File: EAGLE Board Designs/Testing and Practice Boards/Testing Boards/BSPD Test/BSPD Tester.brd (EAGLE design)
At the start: 26.3 x 62.2 mm, 43 parts, among them J1 JUMPER.1, J10 JUMPER.1, J11 JUMPER.1, J12 JUMPER.1, J13 JUMPER.1, J14 JUMPER.1, J15 JUMPER.1, J16 JUMPER.1, J17 JUMPER.1, J18 JUMPER.1, J19 JUMPER.1, J2 JUMPER.1, J20 JUMPER.1, J21 JUMPER.1, J3 JUMPER.1, J4 JUMPER.1, J5 JUMPER.1, J6 JUMPER.1, J7 JUMPER.1, J8 JUMPER.1, J9 JUMPER.1, X1 CONNECTOR-4NANO-FIT-VERTICAL-4

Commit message: final uplaod of rev1 BSPD test board
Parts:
- moved J21 17.8 mm to (3.81, 62.2), turned to 180 degrees
- moved J19 16.3 mm to (15.2, 73.7)
- moved J14 3.81 mm to (3.81, 54.6)
- moved J15 3.81 mm to (3.81, 50.8)
- moved J17 3.81 mm to (3.81, 43.2)
- moved J18 3.81 mm to (3.81, 39.4)
- moved R15 3.81 mm to (8.89, 54.6)
- moved R16 3.81 mm to (8.89, 50.8)
- moved R18 3.81 mm to (8.89, 43.2)
- moved R19 3.81 mm to (8.89, 39.4)
- moved J13 3.81 mm to (3.81, 58.4)
- moved J16 3.81 mm to (3.81, 47.0)
- moved R14 3.81 mm to (8.89, 58.4)
- moved R17 3.81 mm to (8.89, 47.0)
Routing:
- net STUPID2: track 19.0 -> 51.0 mm
- net CURRENT: track 8.02 -> 19.1 mm
- net VCC: track 124.9 -> 131.8 mm
- net STUPID: track 52.0 -> 58.8 mm
- net N$20: track 0.00 -> 6.13 mm
- net BRAKE: track 24.7 -> 21.0 mm

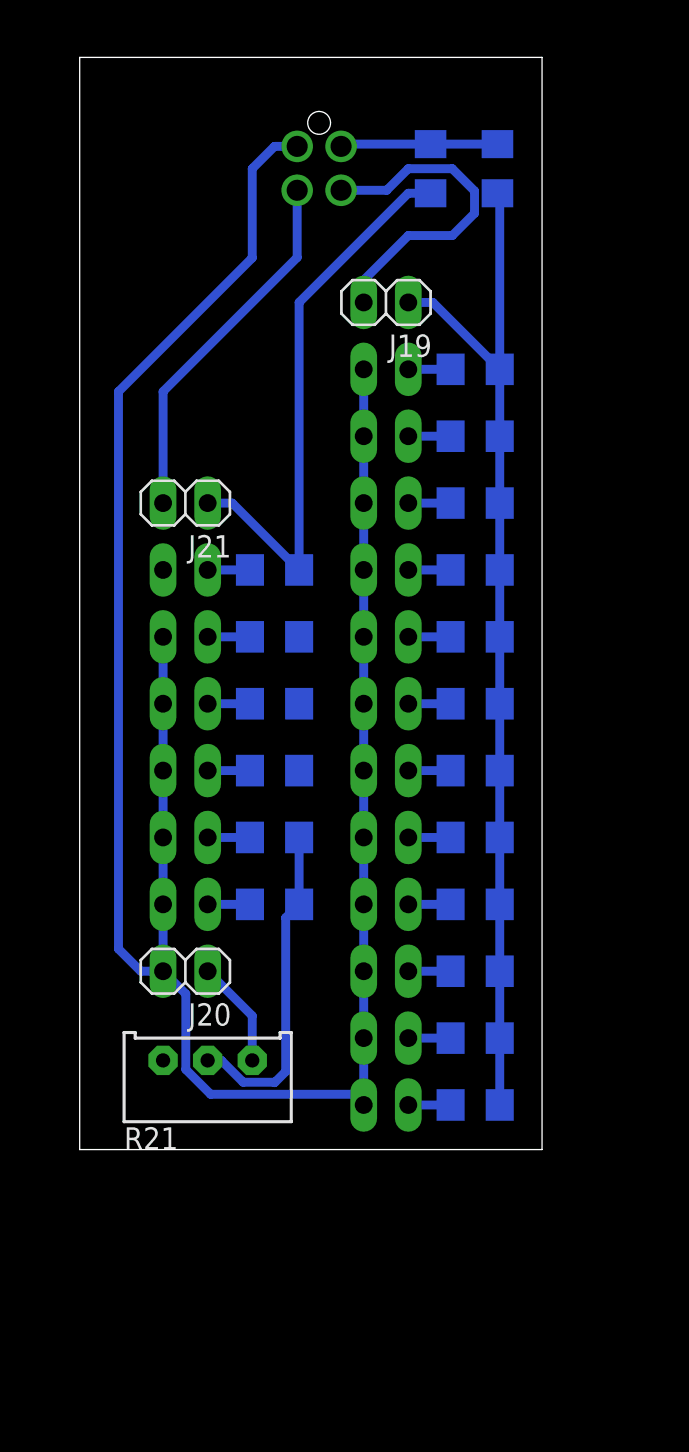
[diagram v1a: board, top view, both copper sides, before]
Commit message: fixed wiring error
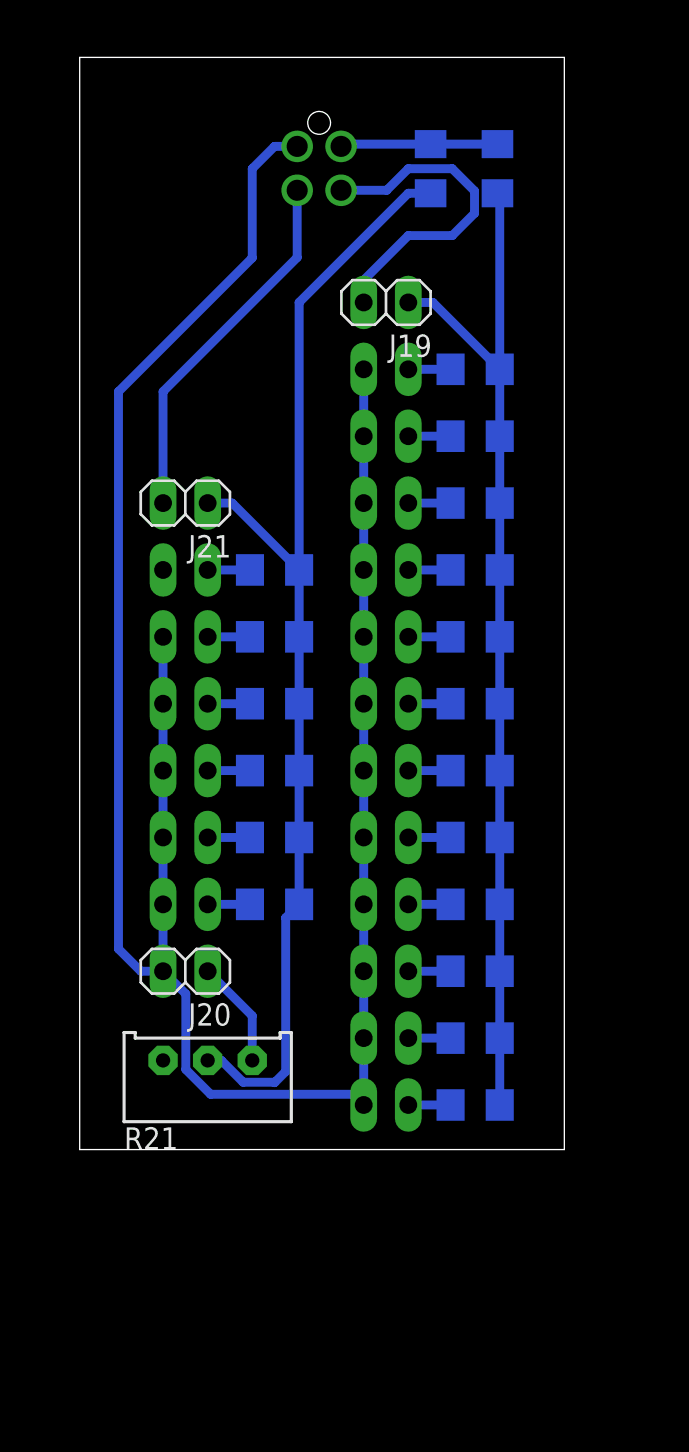
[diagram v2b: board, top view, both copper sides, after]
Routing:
- net STUPID2: track 51.0 -> 66.2 mm
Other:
- board size 26.3 x 62.2 mm -> 27.6 x 62.2 mm
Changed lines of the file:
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@@
 <board>
 <plain>
-<wire x1="24.13" y1="25.4" x2="-2.21" y2="25.4" width="0" layer="20"/>
+<wire x1="25.4" y1="25.4" x2="-2.21" y2="25.4" width="0" layer="20"/>
 <wire x1="-2.21" y1="25.4" x2="-2.21" y2="87.62" width="0" layer="20"/>
-<wire x1="-2.21" y1="87.62" x2="24.13" y2="87.62" width="0" layer="20"/>
-<wire x1="24.13" y1="87.62" x2="24.13" y2="25.4" width="0" layer="20"/>
+<wire x1="-2.21" y1="87.62" x2="25.4" y2="87.62" width="0" layer="20"/>
+<wire x1="25.4" y1="87.62" x2="25.4" y2="25.4" width="0" layer="20"/>
 </plain>
 <attributes>
@@
 <wire x1="5.08" y1="62.23" x2="6.48" y2="62.23" width="0.508" layer="16"/>
 <wire x1="6.48" y1="62.23" x2="10.29" y2="58.42" width="0.508" layer="16"/>
+<wire x1="10.29" y1="58.42" x2="10.29" y2="54.61" width="0.508" layer="16"/>
+<wire x1="10.29" y1="54.61" x2="10.29" y2="50.8" width="0.508" layer="16"/>
+<wire x1="10.29" y1="50.8" x2="10.29" y2="46.99" width="0.508" layer="16"/>
+<wire x1="10.29" y1="46.99" x2="10.29" y2="43.18" width="0.508" layer="16"/>
 </signal>
 </signals>

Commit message: fixed wiring issues and added awp amp
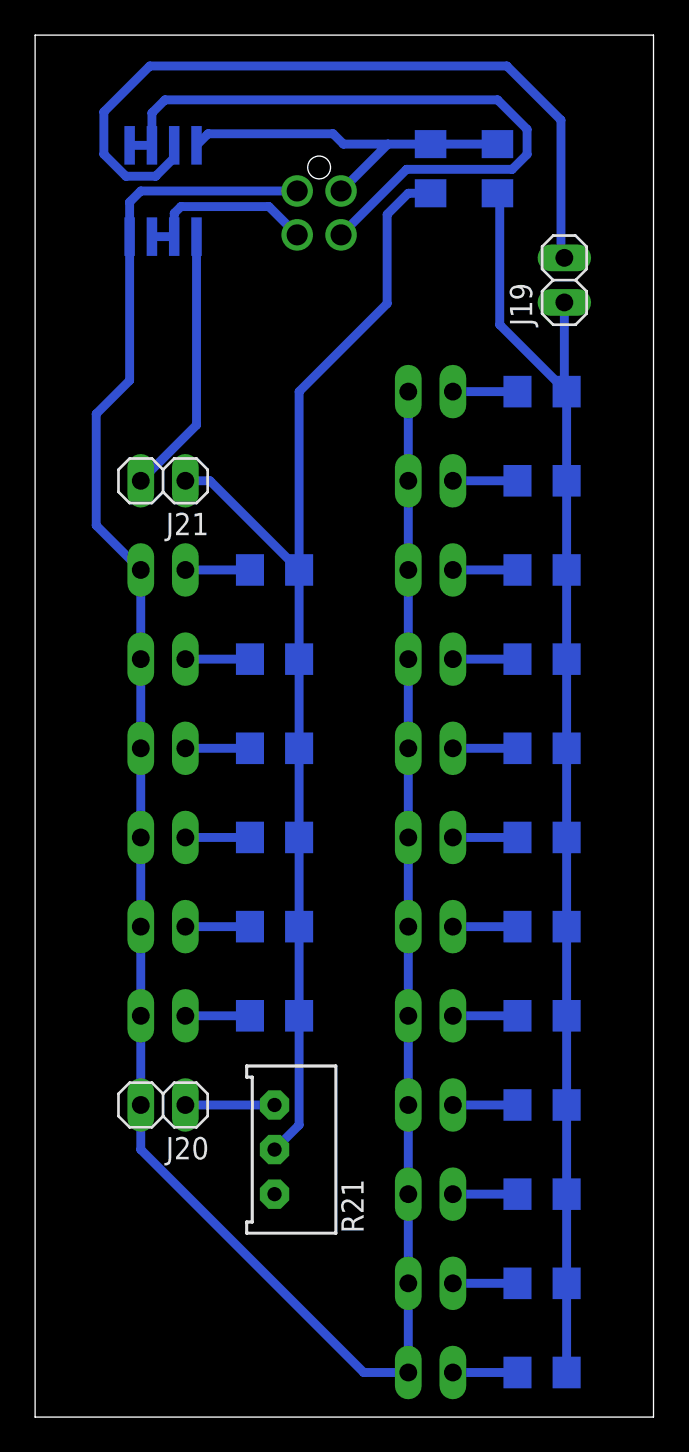
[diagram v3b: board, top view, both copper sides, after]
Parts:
- added U$1: NE5532SOIC, HyTechDevices:SOIC-08
- moved R2 15.7 mm to (24.1, 12.7)
- moved J1 15.5 mm to (17.8, 12.7)
- moved R3 14.5 mm to (24.1, 17.8)
- moved J2 14.2 mm to (17.8, 17.8)
- moved R4 13.3 mm to (24.1, 22.9)
- moved J3 13.0 mm to (17.8, 22.9)
- moved R5 12.0 mm to (24.1, 27.9)
- moved J4 11.7 mm to (17.8, 27.9)
- moved R6 10.9 mm to (24.1, 33.0)
- moved J5 10.5 mm to (17.8, 33.0)
- moved J19 10.2 mm to (25.4, 74.9), turned to 90 degrees
- moved R7 9.67 mm to (24.1, 38.1)
- moved J6 9.25 mm to (17.8, 38.1)
- moved R8 8.52 mm to (24.1, 43.2)
- moved J7 8.03 mm to (17.8, 43.2)
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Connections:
- new net BRAKEOUT: U$1.6, U$1.7, X1.P$3
- new net CURRENTOUT: U$1.1, U$1.2, X1.P$4
- net BRAKE: now also U$1.5; no longer X1.P$3
- net CURRENT: now also U$1.3; no longer X1.P$4
- net GND: now also U$1.4
- net VCC: now also U$1.8
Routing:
- net CURRENTOUT: track 0.00 -> 39.4 mm
- net CURRENT: track 19.1 -> 44.4 mm
- net STUPID: track 58.8 -> 73.9 mm
- net GND: track 8.96 -> 21.4 mm
- net BRAKEOUT: track 0.00 -> 10.4 mm
- net VCC: track 131.8 -> 142.0 mm
- net BRAKE: track 21.0 -> 15.2 mm
- net N$2: track 2.41 -> 3.68 mm
- net N$18: track 2.41 -> 3.68 mm
- net N$17: track 2.41 -> 3.68 mm
- net N$16: track 2.41 -> 3.68 mm
- net N$15: track 2.41 -> 3.68 mm
- net N$14: track 2.41 -> 3.68 mm
- net N$9: track 2.41 -> 3.68 mm
- net N$8: track 2.41 -> 3.68 mm
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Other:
- board size 27.6 x 62.2 mm -> 35.2 x 78.7 mm

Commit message: Updated resistor values to actual rev1 board
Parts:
- R1, R20: value 10K Ohms -> 35.7K Ohms
- R10: value 3.65K Ohms -> 1.87K Ohms
- R11: value 1.21K Ohms -> 604 Ohms
- R14: value 10K Ohms -> 845K Ohms
- R15: value 10K Ohms -> 681K Ohms
- R16: value 10K Ohms -> 499K Ohms
- R17: value 10K Ohms -> 86.6K Ohms
- R18: value 10K Ohms -> 60.4K Ohms
- R19: value 10K Ohms -> 56.2K Ohms
- R2: value 1M Ohms -> 348K Ohms
- R3: value 191K Ohms -> 294K Ohms
- R4: value 97.6K Ohms -> 71.5K Ohms
- R5: value 80.6K Ohms -> 28K Ohms
- R6: value 20K Ohms -> 26.1K Ohms
- R7: value 7.87K Ohms -> 13K Ohms
- R8: value 7.32K Ohms -> 4.32K Ohms
- R9: value 10K Ohms -> 3.57K Ohms
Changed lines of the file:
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@@
 <attribute name="VALUE" x="20.32" y="48.895" size="1.27" layer="28" rot="MR0"/>
 </element>
-<element name="R1" library="HyTechDevices" package="1206" value="10K Ohms" x="21.59" y="81.28" smashed="yes" rot="MR270">
+<element name="R1" library="HyTechDevices" package="1206" value="35.7K Ohms" x="21.59" y="81.28" smashed="yes" rot="MR270">
 <attribute name="NAME" x="20.828" y="82.169" size="0.4064" layer="26" font="vector" rot="MR270"/>
 <attribute name="VALUE" x="22.733" y="82.296" size="0.4064" layer="28" font="vector" rot="MR270"/>
 </element>
-<element name="R10" library="HyTechDevices" package="1206" value="3.65K Ohms" x="24.13" y="53.34" smashed="yes" rot="MR0">
+<element name="R10" library="HyTechDevices" package="1206" value="1.87K Ohms" x="24.13" y="53.34" smashed="yes" rot="MR0">
 <attribute name="NAME" x="25.019" y="54.102" size="0.4064" layer="26" font="vector" rot="MR0"/>
 <attribute name="VALUE" x="25.146" y="52.197" size="0.4064" layer="28" font="vector" rot="MR0"/>
 </element>
-<element name="R11" library="HyTechDevices" package="1206" value="1.21K Ohms" x="24.13" y="58.42" smashed="yes" rot="MR0">
+<element name="R11" library="HyTechDevices" package="1206" value="604 Ohms" x="24.13" y="58.42" smashed="yes" rot="MR0">
 <attribute name="NAME" x="25.019" y="59.182" size="0.4064" layer="26" font="vector" rot="MR0"/>
 <attribute name="VALUE" x="25.146" y="57.277" size="0.4064" layer="28" font="vector" rot="MR0"/>
@@
 <attribute name="VALUE" x="25.146" y="67.437" size="0.4064" layer="28" font="vector" rot="MR0"/>
 </element>
-<element name="R2" library="HyTechDevices" package="1206" value="1M Ohms" x="24.13" y="12.7" smashed="yes" rot="MR0">
+<element name="R2" library="HyTechDevices" package="1206" value="348K Ohms" x="24.13" y="12.7" smashed="yes" rot="MR0">
 <attribute name="NAME" x="25.019" y="13.462" size="0.4064" layer="26" font="vector" rot="MR0"/>
 <attribute name="VALUE" x="25.146" y="11.557" size="0.4064" layer="28" font="vector" rot="MR0"/>
 </element>
-<element name="R3" library="HyTechDevices" package="1206" value="191K Ohms" x="24.13" y="17.78" smashed="yes" rot="MR0">
+<element name="R3" library="HyTechDevices" package="1206" value="294K Ohms" x="24.13" y="17.78" smashed="yes" rot="MR0">
 <attribute name="NAME" x="25.019" y="18.542" size="0.4064" layer="26" font="vector" rot="MR0"/>
 <attribute name="VALUE" x="25.146" y="16.637" size="0.4064" layer="28" font="vector" rot="MR0"/>
 </element>
-<element name="R4" library="HyTechDevices" package="1206" value="97.6K Ohms" x="24.13" y="22.86" smashed="yes" rot="MR0">
+<element name="R4" library="HyTechDevices" package="1206" value="71.5K Ohms" x="24.13" y="22.86" smashed="yes" rot="MR0">
 <attribute name="NAME" x="25.019" y="23.622" size="0.4064" layer="26" font="vector" rot="MR0"/>
 <attribute name="VALUE" x="25.146" y="21.717" size="0.4064" layer="28" font="vector" rot="MR0"/>
 </element>
-<element name="R5" library="HyTechDevices" package="1206" value="80.6K Ohms" x="24.13" y="27.94" smashed="yes" rot="MR0">
+<element name="R5" library="HyTechDevices" package="1206" value="28K Ohms" x="24.13" y="27.94" smashed="yes" rot="MR0">
 <attribute name="NAME" x="25.019" y="28.702" size="0.4064" layer="26" font="vector" rot="MR0"/>
 <attribute name="VALUE" x="25.146" y="26.797" size="0.4064" layer="28" font="vector" rot="MR0"/>
 </element>
-<element name="R6" library="HyTechDevices" package="1206" value="20K Ohms" x="24.13" y="33.02" smashed="yes" rot="MR0">
+<element name="R6" library="HyTechDevices" package="1206" value="26.1K Ohms" x="24.13" y="33.02" smashed="yes" rot="MR0">
 <attribute name="NAME" x="25.019" y="33.782" size="0.4064" layer="26" font="vector" rot="MR0"/>
 <attribute name="VALUE" x="25.146" y="31.877" size="0.4064" layer="28" font="vector" rot="MR0"/>
 </element>
-<element name="R7" library="HyTechDevices" package="1206" value="7.87K Ohms" x="24.13" y="38.1" smashed="yes" rot="MR0">
+<element name="R7" library="HyTechDevices" package="1206" value="13K Ohms" x="24.13" y="38.1" smashed="yes" rot="MR0">
 <attribute name="NAME" x="25.019" y="38.862" size="0.4064" layer="26" font="vector" rot="MR0"/>
 <attribute name="VALUE" x="25.146" y="36.957" size="0.4064" layer="28" font="vector" rot="MR0"/>
 </element>
-<element name="R8" library="HyTechDevices" package="1206" value="7.32K Ohms" x="24.13" y="43.18" smashed="yes" rot="MR0">
+<element name="R8" library="HyTechDevices" package="1206" value="4.32K Ohms" x="24.13" y="43.18" smashed="yes" rot="MR0">
 <attribute name="NAME" x="25.019" y="43.942" size="0.4064" layer="26" font="vector" rot="MR0"/>
 <attribute name="VALUE" x="25.146" y="42.037" size="0.4064" layer="28" font="vector" rot="MR0"/>
 </element>
-<element name="R9" library="HyTechDevices" package="1206" value="10K Ohms" x="24.13" y="48.26" smashed="yes" rot="MR0">
+<element name="R9" library="HyTechDevices" package="1206" value="3.57K Ohms" x="24.13" y="48.26" smashed="yes" rot="MR0">
 <attribute name="NAME" x="25.019" y="49.022" size="0.4064" layer="26" font="vector" rot="MR0"/>
 <attribute name="VALUE" x="25.146" y="47.117" size="0.4064" layer="28" font="vector" rot="MR0"/>
 </element>
-<element name="R14" library="HyTechDevices" package="1206" value="10K Ohms" x="8.89" y="58.42" smashed="yes" rot="MR0">
+<element name="R14" library="HyTechDevices" package="1206" value="845K Ohms" x="8.89" y="58.42" smashed="yes" rot="MR0">
 <attribute name="NAME" x="9.779" y="59.182" size="0.4064" layer="26" font="vector" rot="MR0"/>
 <attribute name="VALUE" x="2.286" y="53.467" size="0.4064" layer="28" font="vector" rot="MR0"/>
 </element>
-<element name="R15" library="HyTechDevices" package="1206" value="10K Ohms" x="8.89" y="53.34" smashed="yes" rot="MR0">
+<element name="R15" library="HyTechDevices" package="1206" value="681K Ohms" x="8.89" y="53.34" smashed="yes" rot="MR0">
 <attribute name="NAME" x="9.779" y="54.102" size="0.4064" layer="26" font="vector" rot="MR0"/>
 <attribute name="VALUE" x="9.906" y="52.197" size="0.4064" layer="28" font="vector" rot="MR0"/>
 </element>
-<element name="R16" library="HyTechDevices" package="1206" value="10K Ohms" x="8.89" y="48.26" smashed="yes" rot="MR0">
+<element name="R16" library="HyTechDevices" package="1206" value="499K Ohms" x="8.89" y="48.26" smashed="yes" rot="MR0">
 <attribute name="NAME" x="9.779" y="49.022" size="0.4064" layer="26" font="vector" rot="MR0"/>
 <attribute name="VALUE" x="9.906" y="47.117" size="0.4064" layer="28" font="vector" rot="MR0"/>
 </element>
-<element name="R17" library="HyTechDevices" package="1206" value="10K Ohms" x="8.89" y="43.18" smashed="yes" rot="MR0">
+<element name="R17" library="HyTechDevices" package="1206" value="86.6K Ohms" x="8.89" y="43.18" smashed="yes" rot="MR0">
 <attribute name="NAME" x="9.779" y="43.942" size="0.4064" layer="26" font="vector" rot="MR0"/>
 <attribute name="VALUE" x="9.906" y="42.037" size="0.4064" layer="28" font="vector" rot="MR0"/>
 </element>
-<element name="R18" library="HyTechDevices" package="1206" value="10K Ohms" x="8.89" y="38.1" smashed="yes" rot="MR0">
+<element name="R18" library="HyTechDevices" package="1206" value="60.4K Ohms" x="8.89" y="38.1" smashed="yes" rot="MR0">
 <attribute name="NAME" x="9.779" y="38.862" size="0.4064" layer="26" font="vector" rot="MR0"/>
 <attribute name="VALUE" x="9.906" y="36.957" size="0.4064" layer="28" font="vector" rot="MR0"/>
 </element>
-<element name="R19" library="HyTechDevices" package="1206" value="10K Ohms" x="8.89" y="33.02" smashed="yes" rot="MR0">
+<element name="R19" library="HyTechDevices" package="1206" value="56.2K Ohms" x="8.89" y="33.02" smashed="yes" rot="MR0">
 <attribute name="NAME" x="9.779" y="33.782" size="0.4064" layer="26" font="vector" rot="MR0"/>
 <attribute name="VALUE" x="9.906" y="31.877" size="0.4064" layer="28" font="vector" rot="MR0"/>
@@
 <attribute name="VALUE" x="5.08" y="28.575" size="1.27" layer="28" rot="MR0"/>
 </element>
-<element name="R20" library="HyTechDevices" package="1206" value="10K Ohms" x="17.78" y="81.28" smashed="yes" rot="MR270">
+<element name="R20" library="HyTechDevices" package="1206" value="35.7K Ohms" x="17.78" y="81.28" smashed="yes" rot="MR270">
 <attribute name="NAME" x="17.018" y="82.169" size="0.4064" layer="26" font="vector" rot="MR270"/>
 <attribute name="VALUE" x="18.923" y="79.756" size="0.4064" layer="28" font="vector" rot="MR270"/>
